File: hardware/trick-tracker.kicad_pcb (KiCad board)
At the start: 4 copper layers, 31 x 45 mm, 58 parts, among them J1 USB4105-GF-A, J2 S2B-PH-K, J3 QWiiC, J4 MEM2061-01-188-00-A, J6 QWiiC, P1 SMTB-1240-S-R, U1 MS88SF2, U2 DPS368XTSA1, U3 LSM9DS1, U4 MCP73831/OT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

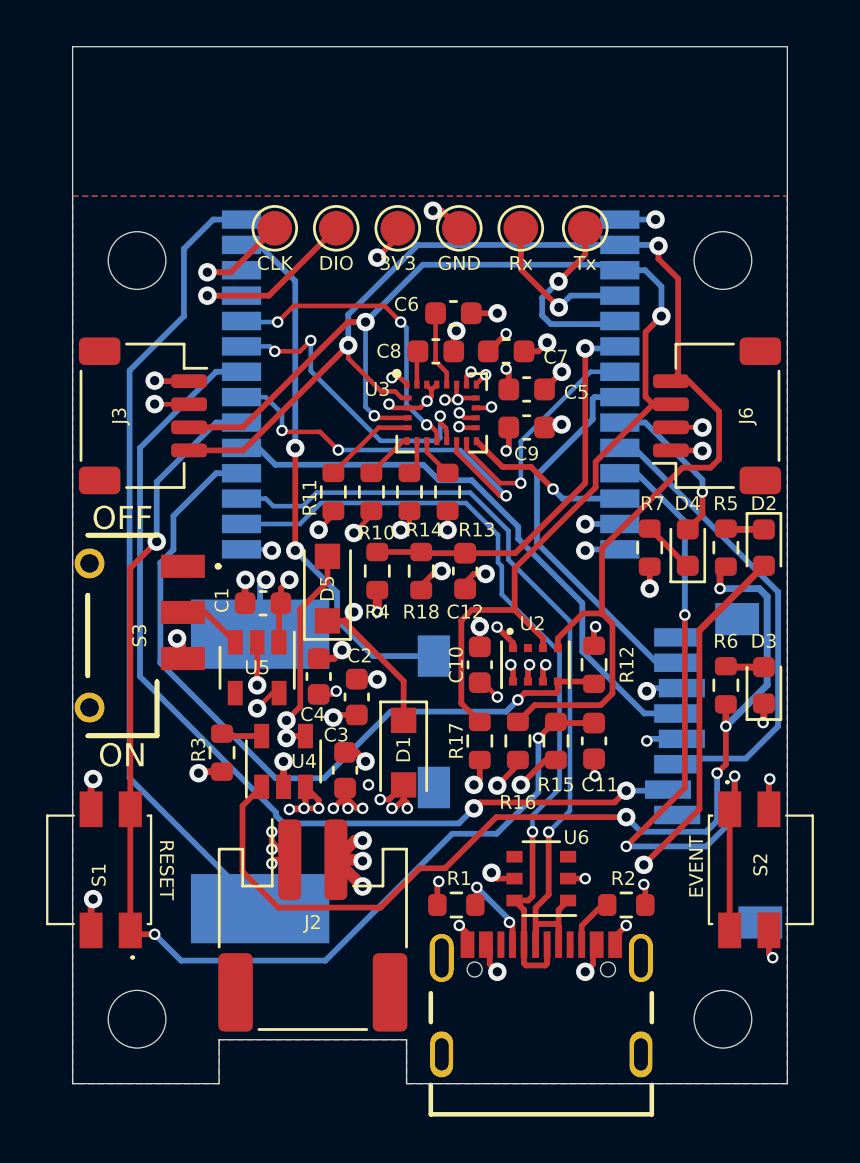
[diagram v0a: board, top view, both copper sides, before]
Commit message: Small adjustments + rounded corners + BOM HTML
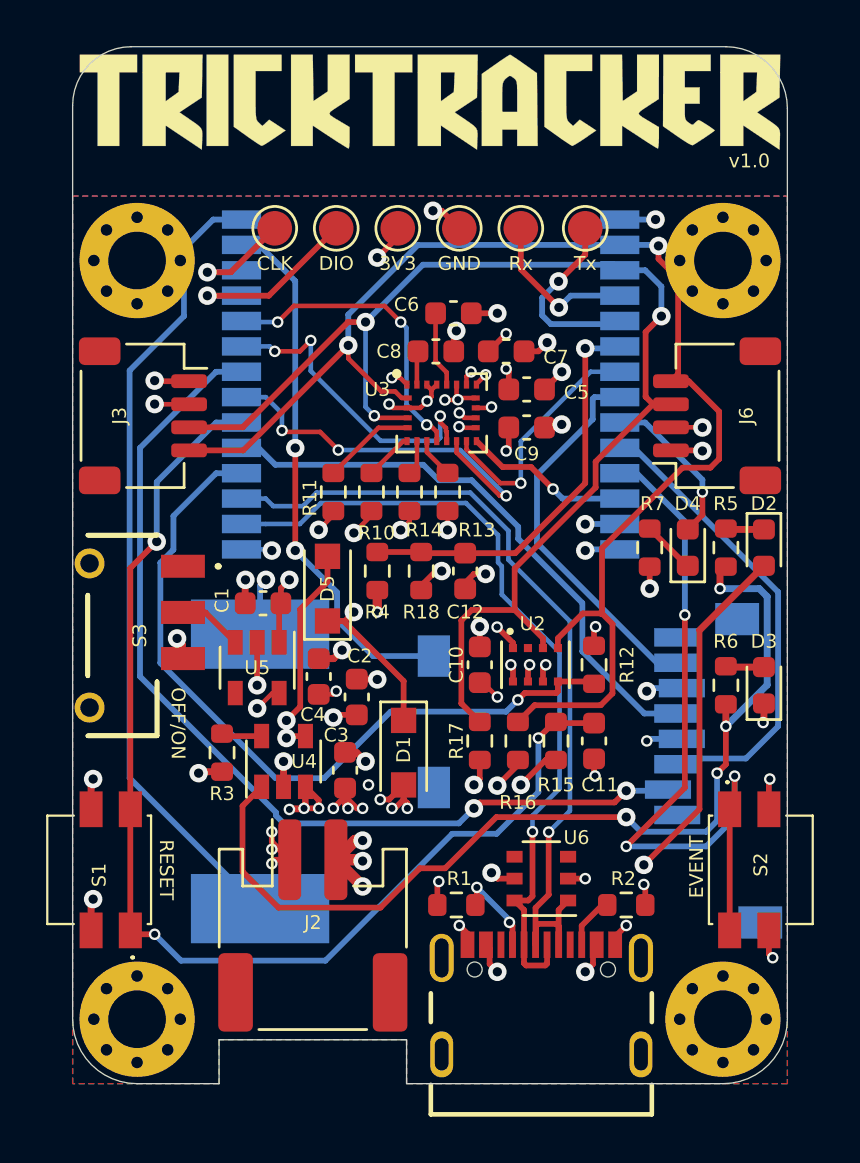
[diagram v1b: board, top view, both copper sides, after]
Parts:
- added G***: LOGO, logo:logo, F.Cu at (145.5, 94.5)
- added REF**: OSHW-Symbol_6.7x6mm_SilkScreen, Symbol:OSHW-Symbol_6.7x6mm_SilkScreen, B.Cu at (150.4, 133.7)
- H1, H2, H3, H4: footprint MountingHole:MountingHole_2.5mm -> MountingHole:MountingHole_2.5mm_Pad_Via
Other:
- outline, holes or cut-outs redrawn
- board text added: "OFF/ON"
- board text added: "v1.0"
- board text removed: "OFF"
- board text removed: "ON"

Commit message: Add connector (placeholder) + extra GND TP
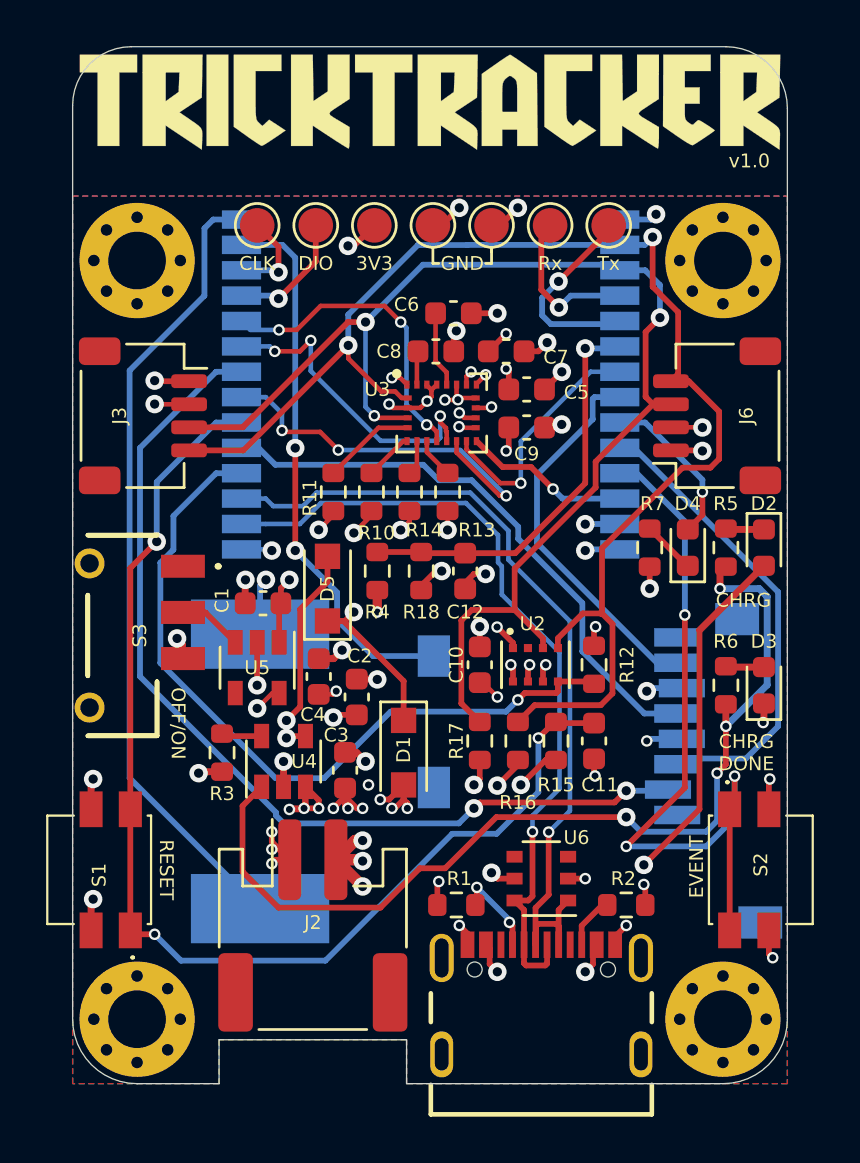
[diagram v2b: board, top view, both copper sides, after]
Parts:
- added TP7: TP_GND, TestPoint:TestPoint_Pad_D1.5mm, F.Cu at (148.2, 99.8)
- moved TP2 1.28 mm to (150.7, 99.8)
- moved TP6 1.15 mm to (145.7, 99.8)
- moved TP5 1.02 mm to (143.1, 99.8)
- moved TP1 1.02 mm to (153.3, 99.8)
- moved TP4 0.90 mm to (140.6, 99.8)
- moved TP3 0.77 mm to (138.0, 99.8)
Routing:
- net /SWDIO: track 8.28 -> 5.50 mm
- net GND: track 53.5 -> 55.1 mm, vias 47 -> 48
- net /SWDCLK: track 5.23 -> 4.29 mm
- net /SD_DETECT: track 23.3 -> 23.9 mm
- net /Tx: track 8.13 -> 8.68 mm
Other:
- board text added: "CHRG"
- board text added: "CHRG DONE"

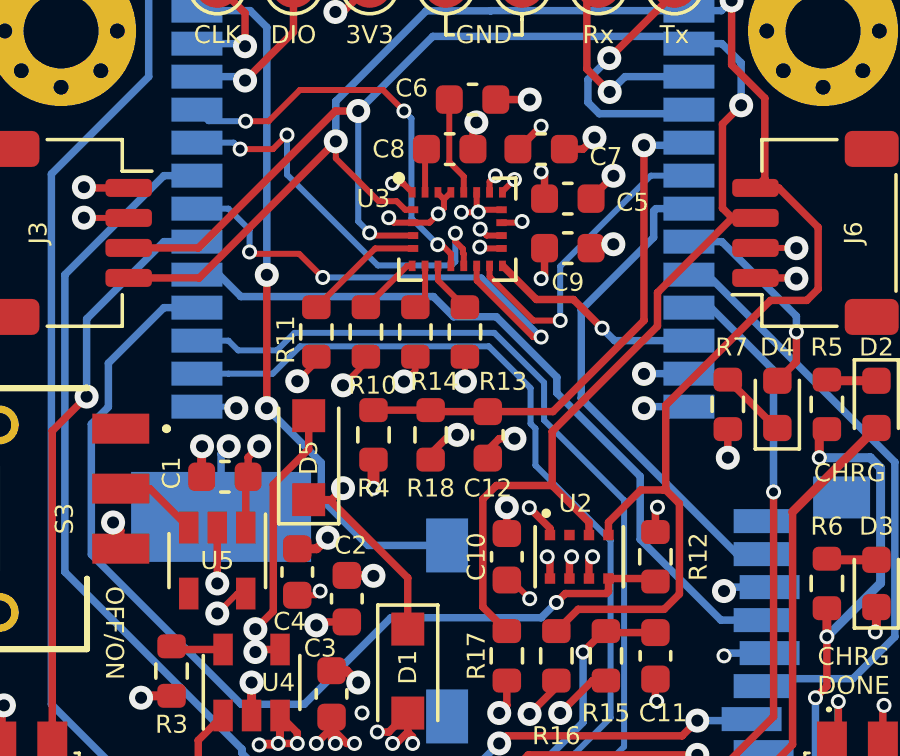
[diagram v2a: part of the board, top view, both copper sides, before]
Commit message: Added Labels
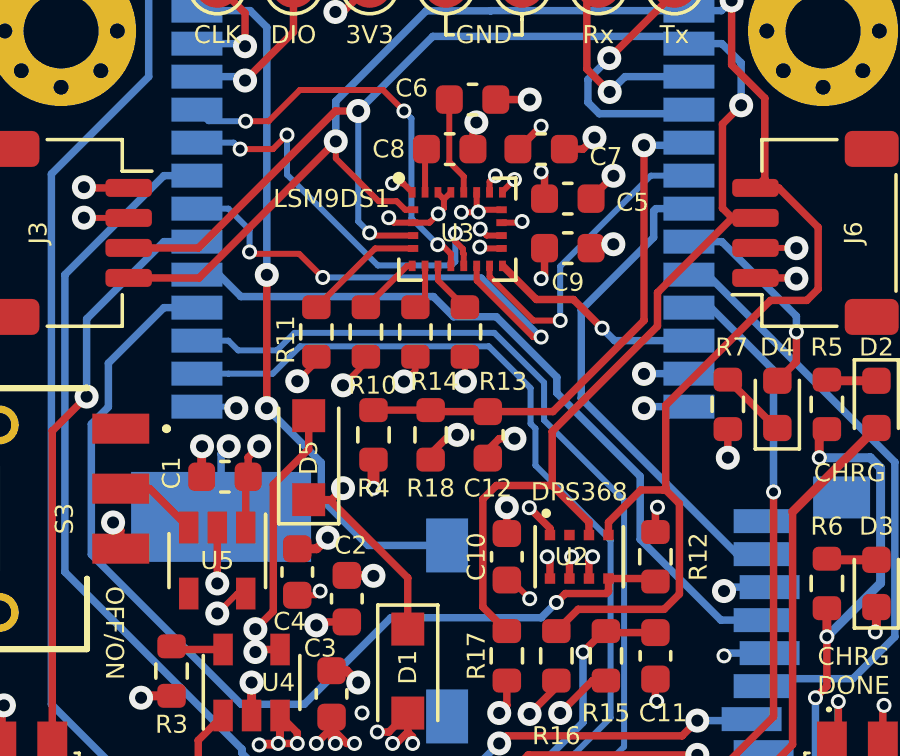
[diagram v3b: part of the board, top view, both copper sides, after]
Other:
- board text added: "DPS368"
- board text added: "LSM9DS1"
